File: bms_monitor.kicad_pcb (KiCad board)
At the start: 2 copper layers, 115 x 65 mm, 238 parts, among them CN1 10nF, CN10 10nF, CN11 10nF, CN12 10nF, CN13 10nF, CN14 10nF, CN2 10nF, CN3 10nF, CN4 10nF, CN5 10nF, CN6 10nF, CN7 10nF, CN8 10nF, CN9 10nF, J1 Conn_01x02, J10 TEMP0, J11 TEMP1, J12 Conn_01x05, J13 Conn_ARM_JTAG_SWD_10, J2 Conn_01x02, J3 Conn_01x02, J4 Conn_01x02, J5 CELLS, J6 TEMP0, J7 TEMP1, J8 Conn_01x05, J9 CELLS, Q1 NSV1C201MZ4, Q2 NSV1C201MZ4, U1 STM32L432KBUx, U10 CD74HC4067SM, U11 MP4541, U12 SM91502ALA, U13 SM91502ALA, U14 SM91502ALA, U3 DSC61XX, U4 TFBS4652, U5 LTC6811-1, U6 CD74HC4067SM, U7 MP4541, U8 SM91502ALA, U9 LTC6811-1

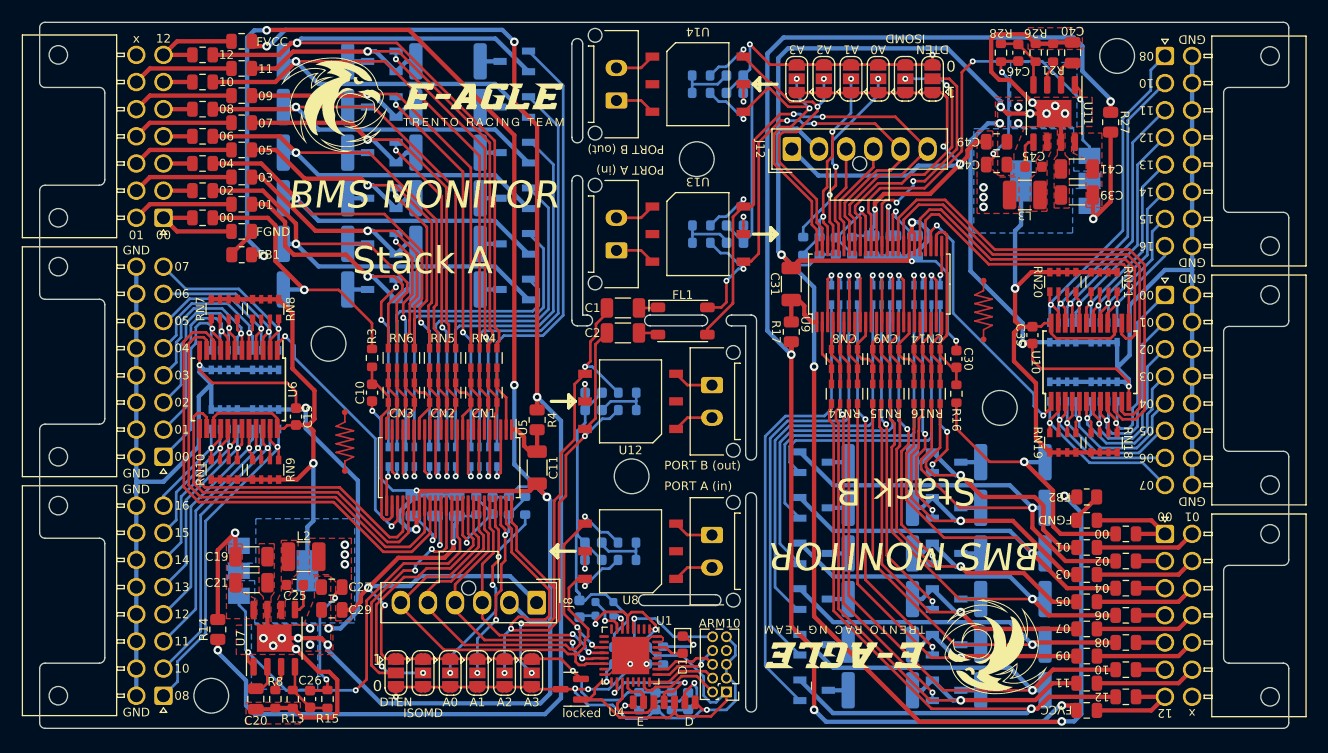
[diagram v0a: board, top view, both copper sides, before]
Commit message: Fixed issure #2
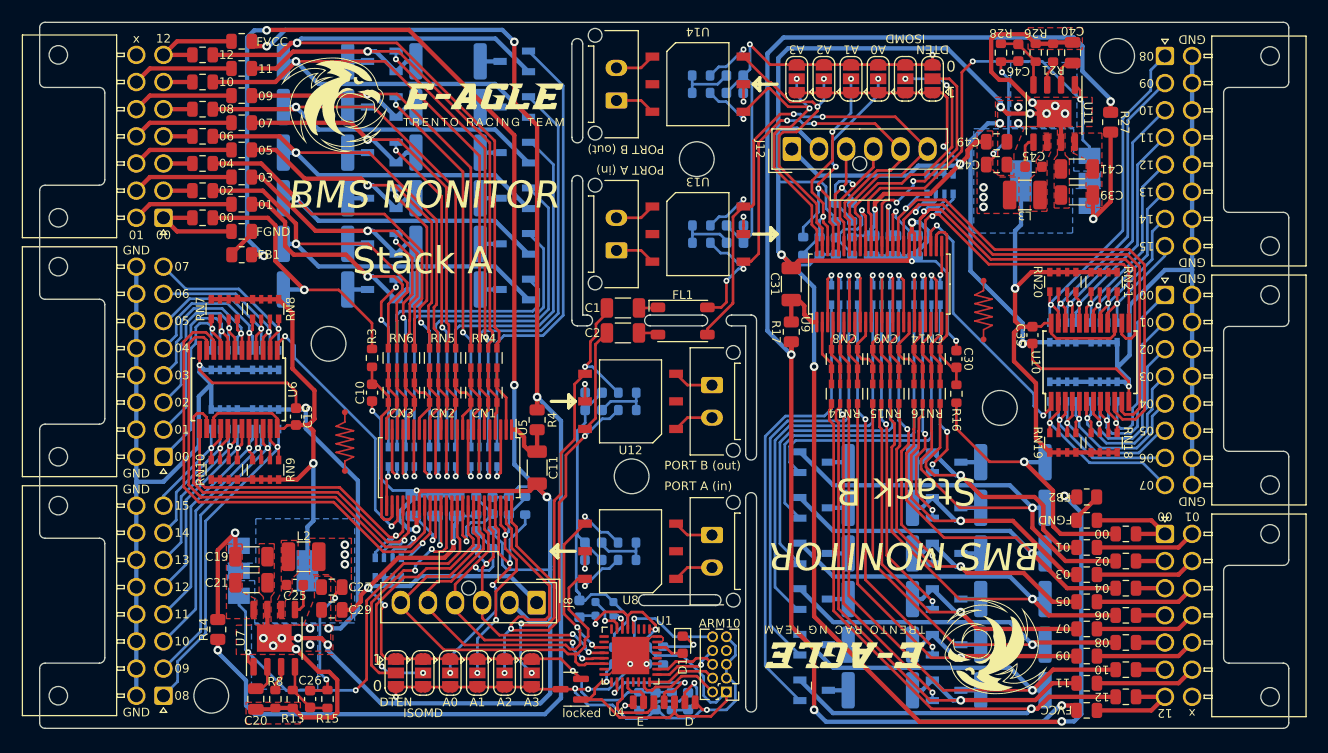
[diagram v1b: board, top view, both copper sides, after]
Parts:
- added R30: R, Resistor_SMD:R_0603_1608Metric, B.Cu at (120.2, 109.6)
- added R31: R, Resistor_SMD:R_0603_1608Metric, B.Cu at (121.7, 109.6)
- added R32: R, Resistor_SMD:R_0603_1608Metric, B.Cu at (154.8, 79.5)
- added R33: R, Resistor_SMD:R_0603_1608Metric, B.Cu at (153.3, 79.5)
- added RN17: 3.3K, Resistor_SMD:R_Array_Convex_4x0603, B.Cu at (112.1, 112.2)
- added RN22: 3.3K, Resistor_SMD:R_Array_Convex_4x0603, B.Cu at (162.9, 76.9)
- J12, J8: value Conn_01x05 -> DIRECT_SPI
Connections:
- net /StackB/SDI renamed /StackB/ICMP_2
- net /StackB/SDO renamed /StackB/IBIAS_2
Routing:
- net GND: track 412.3 -> 420.5 mm
- net /StackB/GND: track 355.3 -> 363.5 mm
- net /StackB/ICMP_2: track 10.4 -> 16.4 mm, vias 0 -> 1
- net /MOSI: track 27.0 -> 33.1 mm, vias 2 -> 3
- net /StackB/MUX_A2: track 33.5 -> 38.0 mm, vias 0 -> 1
- net /StackB/VCC: track 125.9 -> 129.5 mm
- net +5V: track 142.4 -> 146.0 mm
- net /StackA/MUX_A1: track 43.0 -> 46.5 mm, vias 0 -> 1
- net /StackB/MUX_A1: track 43.0 -> 46.3 mm, vias 0 -> 1
- net /StackA/MUX_A2: track 33.5 -> 36.8 mm, vias 0 -> 1
- net /StackB/MUX_A3: track 28.3 -> 31.4 mm, vias 0 -> 1
- net /StackA/MUX_A3: track 28.3 -> 31.4 mm, vias 0 -> 1
- net /StackA/MUX_A0: track 46.1 -> 48.8 mm, vias 0 -> 1
- net /StackB/MUX_A0: track 46.1 -> 48.8 mm, vias 0 -> 1
- net /StackB/IBIAS_2: track 9.48 -> 11.3 mm, vias 0 -> 1
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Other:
- board text removed: "16"

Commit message: addressed swapped collector emitter of Q1
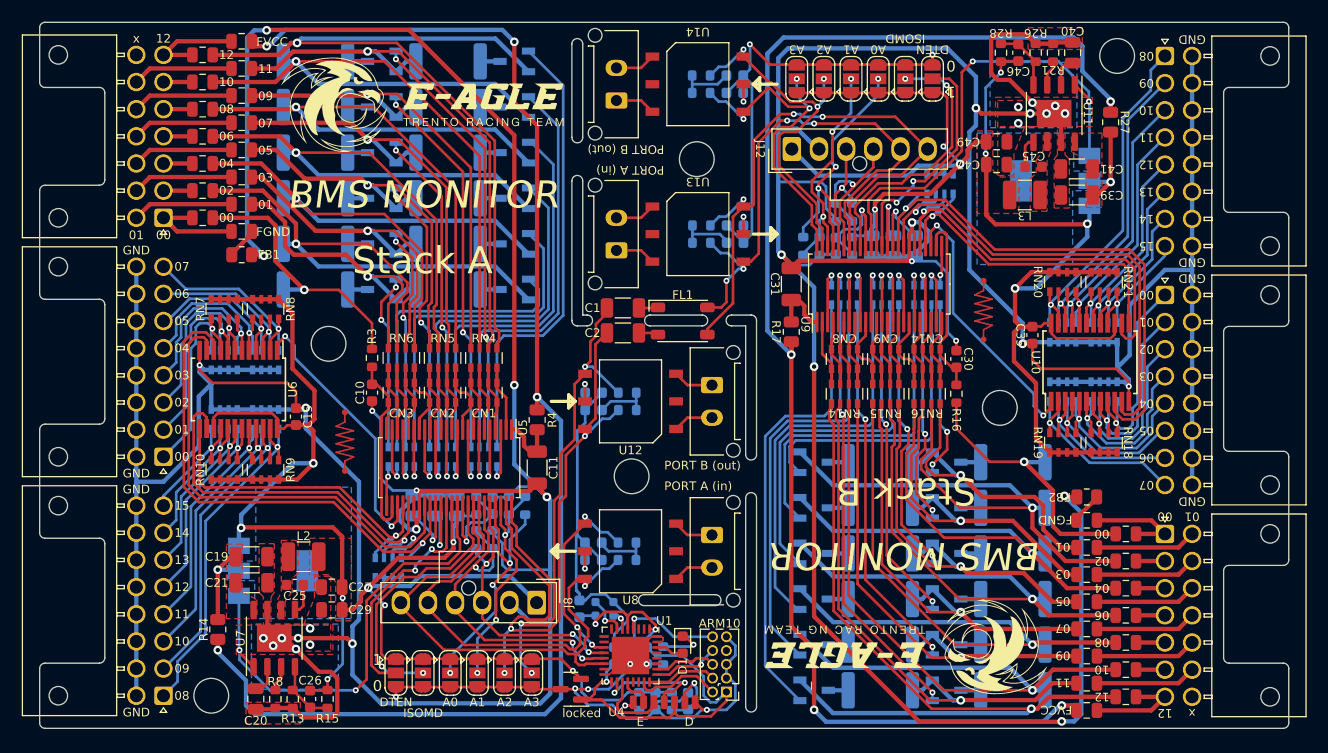
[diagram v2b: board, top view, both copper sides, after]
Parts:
- Q1, Q2: footprint Package_TO_SOT_SMD:SOT-223-3_TabPin2 -> Package_TO_SOT_SMD:SOT-223
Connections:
- Q1 pad 2: +5V -> /StackA/PSU_INPUT
- Q1 pad 3: /StackA/PSU_INPUT -> +5V
- Q2 pad 2: /StackB/VCC -> /StackB/PSU_INPUT
- Q2 pad 3: /StackB/PSU_INPUT -> /StackB/VCC
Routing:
- net +5V: track 146.0 -> 161.7 mm, vias 10 -> 8
- net /StackB/VCC: track 129.5 -> 145.2 mm, vias 9 -> 7
- net /StackA/PSU_INPUT: track 12.2 -> 8.70 mm
- net /StackB/PSU_INPUT: track 12.2 -> 8.70 mm
- net /StackA/DRIVE: track 41.9 -> 43.3 mm
- net /StackB/DRIVE: track 41.9 -> 43.3 mm
- net GND: track 420.5 -> 421.9 mm, vias 24 -> 23
- net /StackB/GND: track 363.5 -> 364.9 mm, vias 20 -> 19
- added copper zone on B.Cu, net /StackA/PSU_INPUT
- added copper zone on B.Cu, net /StackB/PSU_INPUT
- removed copper zone on B.Cu, net +5V
- removed copper zone on B.Cu, net /StackB/VCC

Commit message: changed to bigger footprint for HV caps
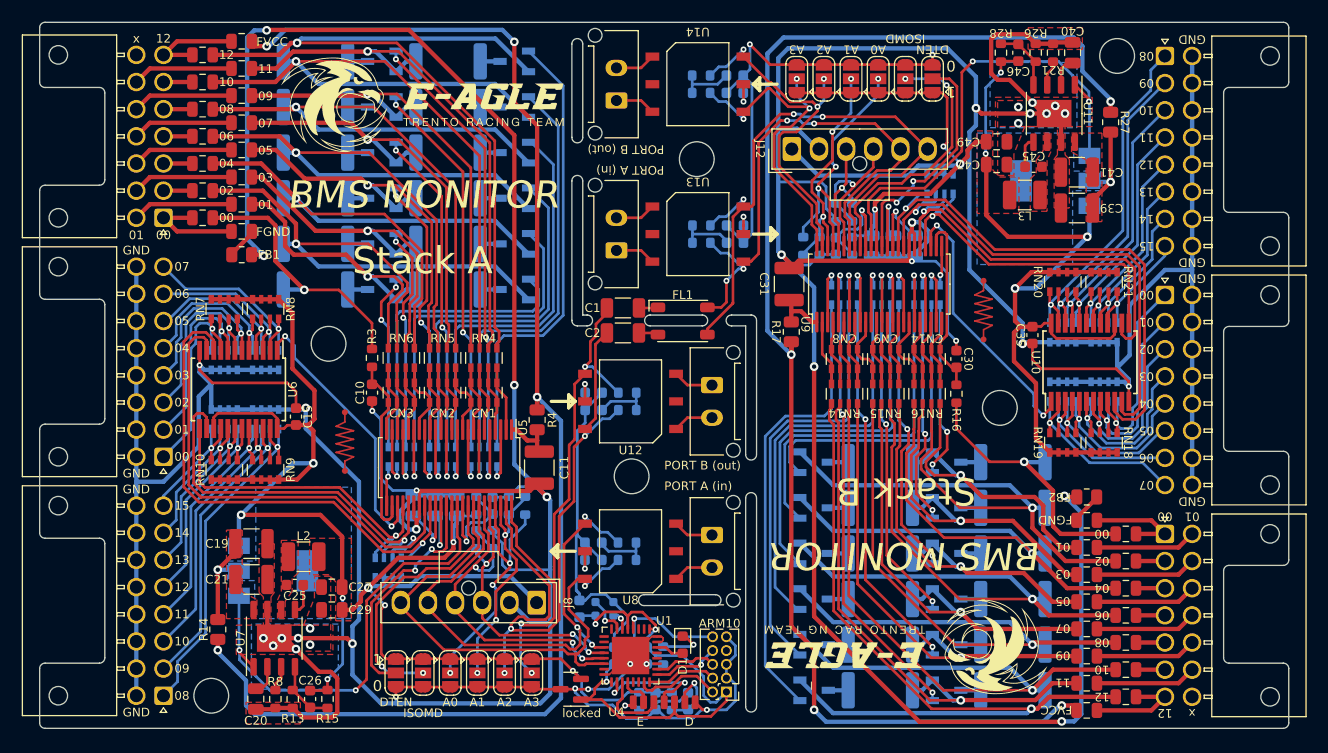
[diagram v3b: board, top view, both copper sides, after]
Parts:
- C11, C19, C21, C31, C39, C41: footprint Capacitor_SMD:C_1206_3216Metric -> Capacitor_SMD:C_1210_3225Metric
- moved C19 1.20 mm to (99.5, 110.0)
- moved C39 1.20 mm to (175.5, 79.1)
- moved C21 0.30 mm to (99.5, 113.3)
- moved C41 0.30 mm to (175.5, 75.8)
- moved C11 0.20 mm to (126.0, 103.0)
- moved C31 0.20 mm to (149.0, 86.1)
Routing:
- net Net-(U5-V+): track 5.62 -> 4.73 mm
- net Net-(U9-V+): track 5.62 -> 4.73 mm

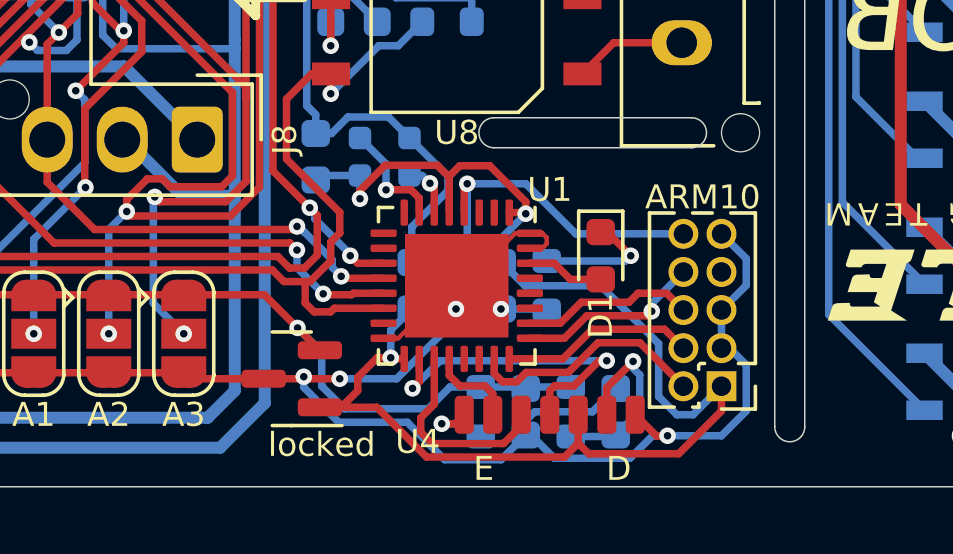
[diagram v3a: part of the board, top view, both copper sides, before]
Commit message: changed SWD connector to smd
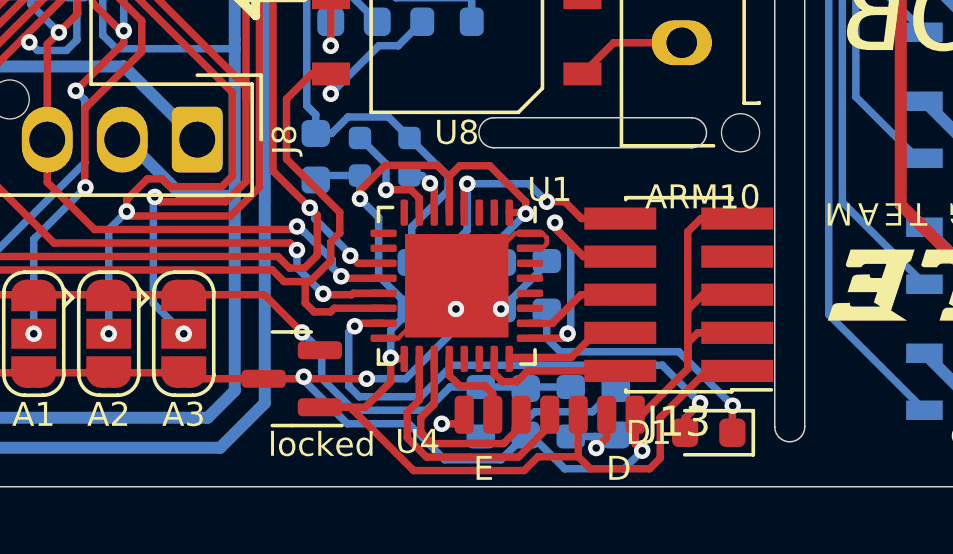
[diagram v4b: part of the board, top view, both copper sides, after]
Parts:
- J13: footprint Connector_PinHeader_1.27mm:PinHeader_2x05_P1.27mm_Vertical -> Connector_PinHeader_1.27mm:PinHeader_2x05_P1.27mm_Vertical_SMD
- moved D1 6.91 mm to (142.8, 125.2), turned to 180 degrees
- moved J13 3.37 mm to (141.8, 120.6)
- turned R29 to 90 degrees
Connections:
- net Net-(U1-PA10) renamed /RX
- net Net-(U1-PA9) renamed /TX
- U1 pad 15: unconnected-(U1-PB1-Pad15) -> Net-(D1-A)
- U1 pad 30: Net-(D1-A) -> unconnected-(U1-PB7-Pad30)
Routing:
- net Net-(D1-A): track 2.59 -> 17.1 mm, vias 0 -> 2
- net Net-(D1-K): track 4.20 -> 8.96 mm
- net +3.3V: track 46.7 -> 42.4 mm
- net GND: track 421.9 -> 425.5 mm
- net Net-(U4-VCC): track 6.54 -> 3.18 mm
- net /SWDIO: track 8.04 -> 4.95 mm
- net Net-(U1-PA8): track 11.0 -> 8.61 mm, vias 2 -> 0
- net /SWCLK: track 6.47 -> 4.06 mm
- net /SWO: track 5.76 -> 3.41 mm
- net /~{RESET}: track 11.7 -> 9.35 mm, vias 1 -> 2
- net /TDI: track 6.18 -> 8.03 mm, vias 1 -> 2
- net +5V: track 162.2 -> 161.0 mm
